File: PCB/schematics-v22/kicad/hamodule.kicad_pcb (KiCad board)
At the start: 2 copper layers, 78.4 x 84.3 mm, 91 parts, among them J1 GND|5V, J10 Conn_01x02_Male, J11 USB_C_Receptacle_USB2.0, J12 2604-1104, J13 EspSense, J2 2604-1102, J3 Conn_01x02_Male, J4 USB | PS, J5 Conn_01x02_Male, J6 GND|3.3V, J7 Current Jumper, J8 EspRelays, J9 2604-1104, K1 AQG12205, K2 AQG12205, K3 AQG12205, K4 AQG12205, SW1 Switch, SW2 Switch, U1 LD1117AV33, U2 ESP32-S3-WROOM-2, U3 ULN2003A, U4 USBLC6-2SC6, U5 LDA210-PDIP, U6 LDA210-PDIP, U7 SHT4x

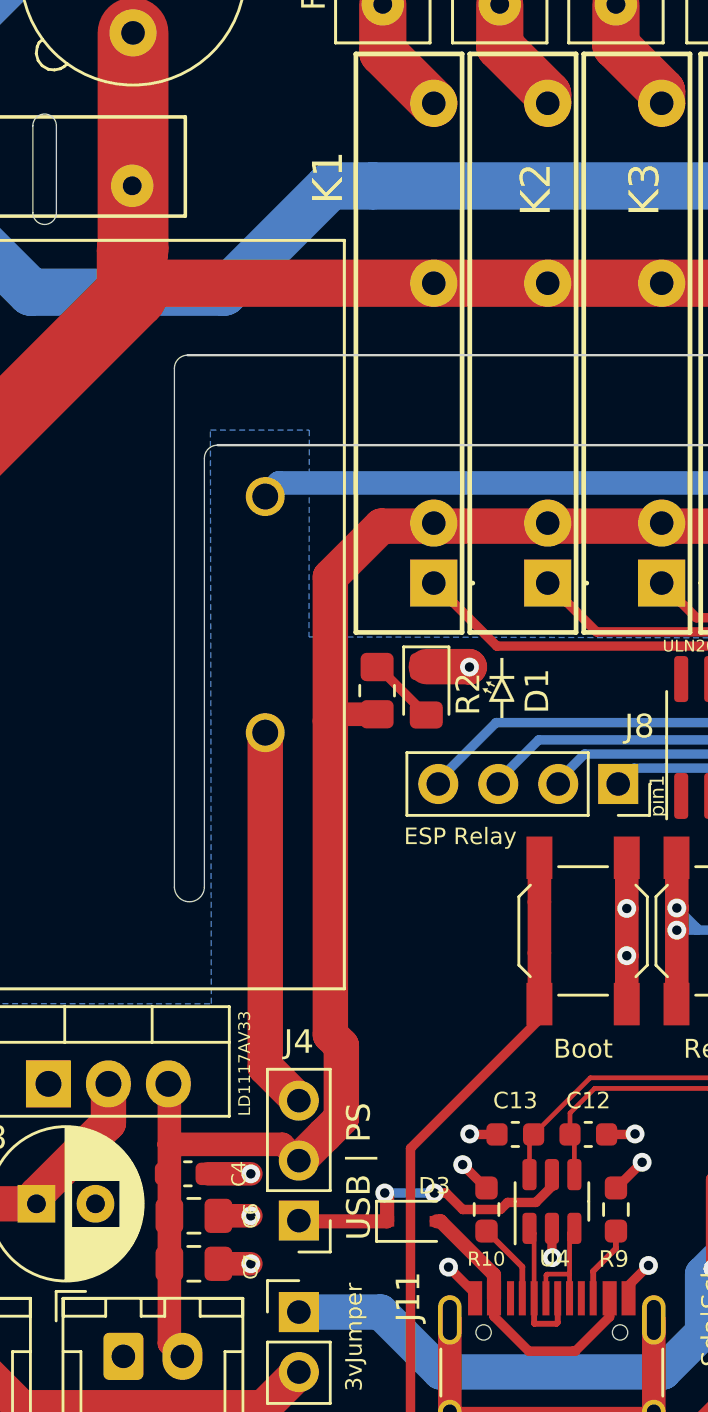
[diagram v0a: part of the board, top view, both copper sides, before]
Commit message: improving schematics, removing global variables and use wires instead to make it clear how the circuit is working; trying to move inputs to the left, output to the right
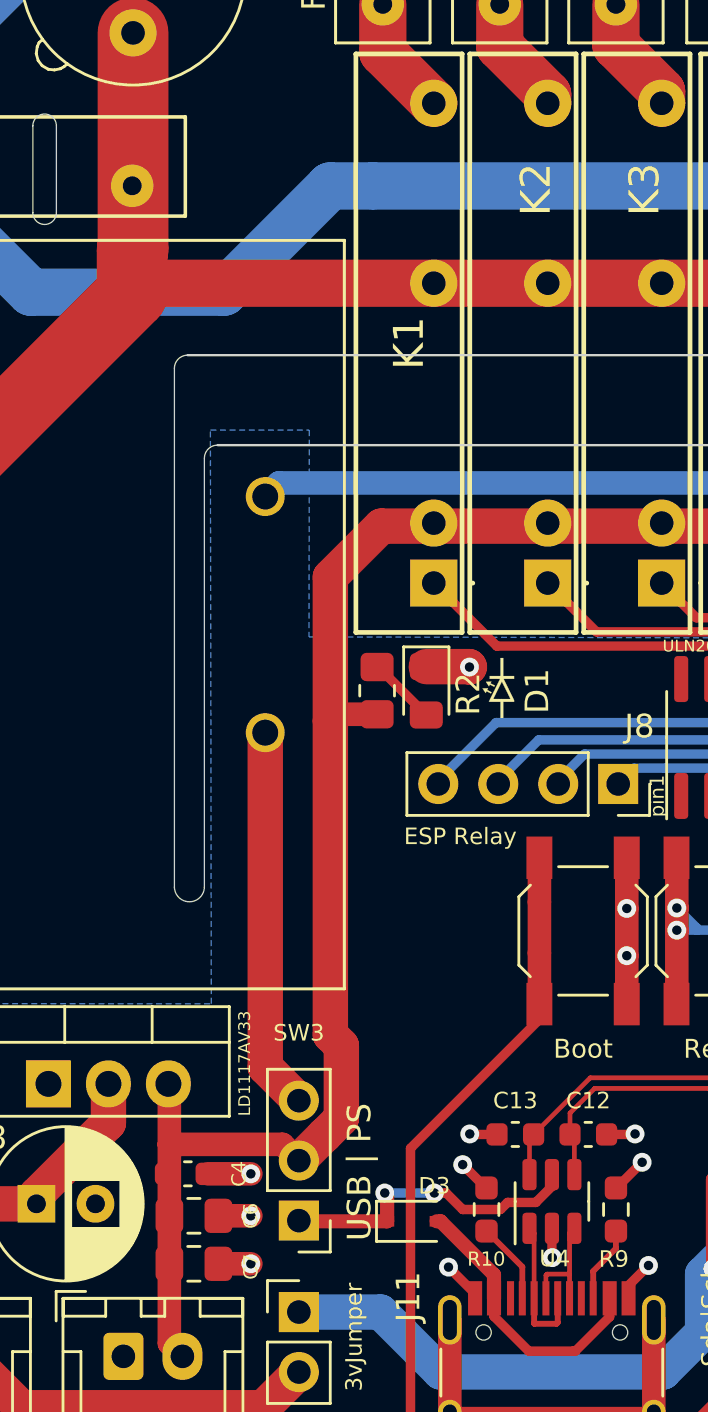
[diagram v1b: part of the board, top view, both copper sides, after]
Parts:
- removed J4: USB | PS, Connector_PinHeader_2.54mm:PinHeader_1x03_P2.54mm_Vertical
- added SW3: USB | PS, Connector_PinHeader_2.54mm:PinHeader_1x03_P2.54mm_Vertical, F.Cu at (56.3, 104.5)
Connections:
- net L_INPUT renamed Net-(F1-Pad1)
- net REI1 renamed Net-(U3-Pad13)
- net REI2 renamed Net-(K2-Pad1)
- net REI3 renamed Net-(K3-Pad1)
- net REI4 renamed Net-(K4-Pad1)
- net REO1 renamed Net-(F2-Pad1)
- net REO2 renamed Net-(F3-Pad1)
- net REO3 renamed Net-(F4-Pad1)
- net REO4 renamed Net-(F5-Pad1)
- net Sens1 renamed Net-(J12-Pad7)
- net Sens2 renamed Net-(J12-Pad5)
- net Sens3 renamed Net-(F8-Pad2)
- net Sens4 renamed Net-(J12-Pad1)
- net USB-D+ renamed Net-(J11-PadA6)
- net USB-D- renamed Net-(J11-PadA7)

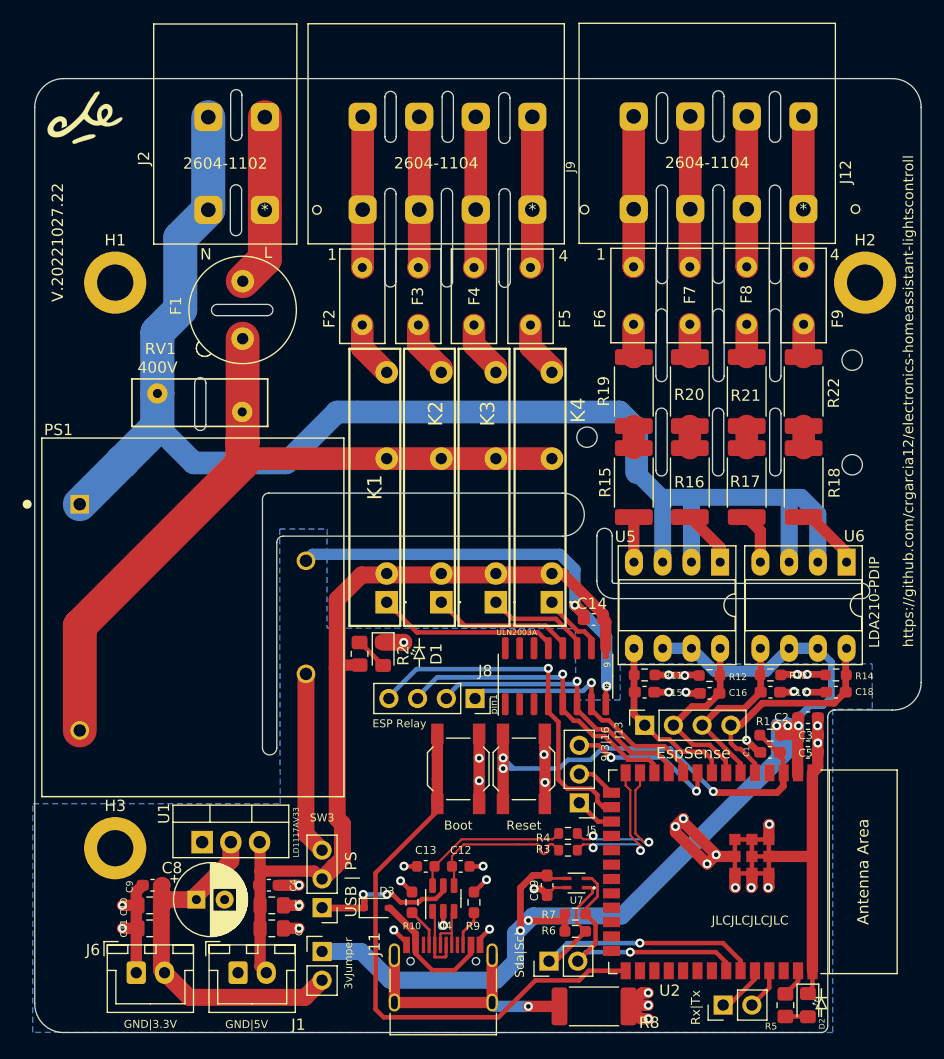
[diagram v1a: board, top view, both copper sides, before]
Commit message: [V22] Making schematics cleaner + Production files
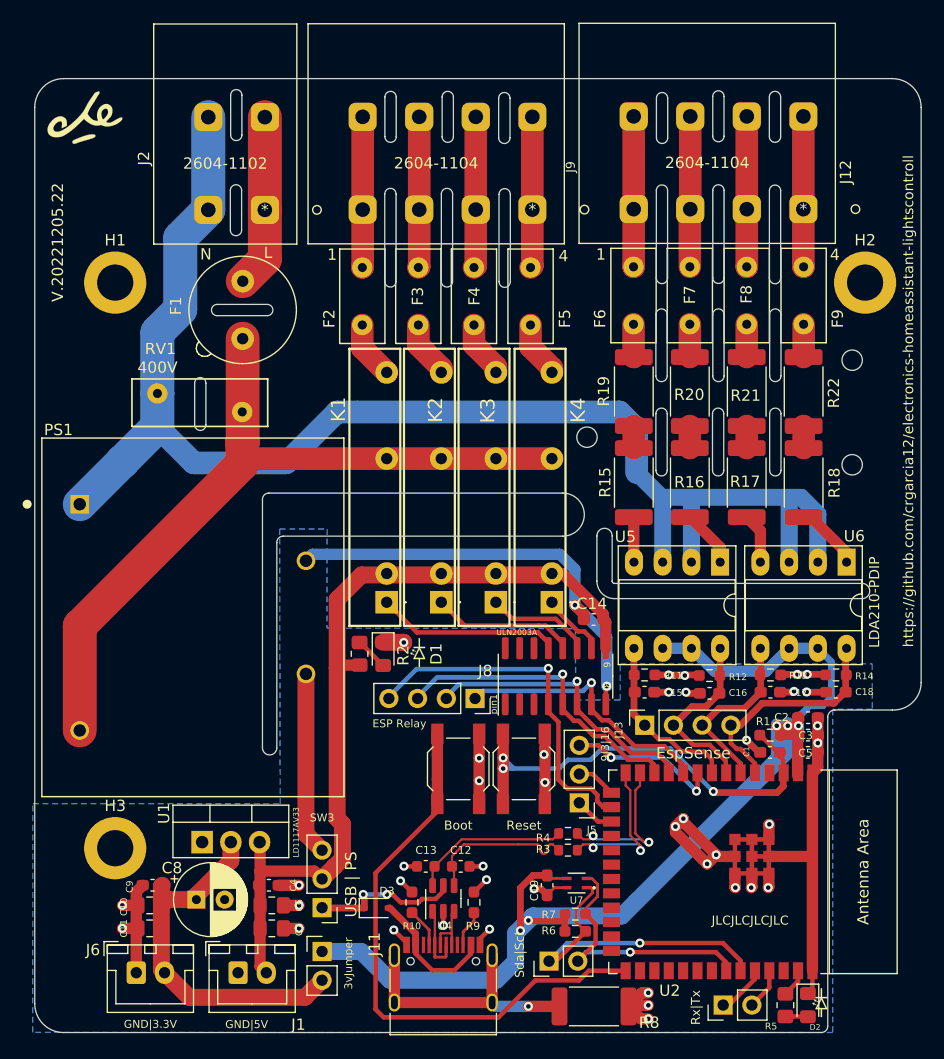
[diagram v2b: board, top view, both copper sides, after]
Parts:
- J10: value Conn_01x02_Male -> Serial
- J3: value Conn_01x02_Male -> Ì2C
- J5: value Conn_01x02_Male -> GPIOs
- turned C13 to 180 degrees
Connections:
- C13 pad 1: GND -> D-
- C13 pad 2: D- -> GND
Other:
- board text added: "V.20221205.22"
- board text removed: "V.20221027.22"

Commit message: adding leds to indicate relays operation
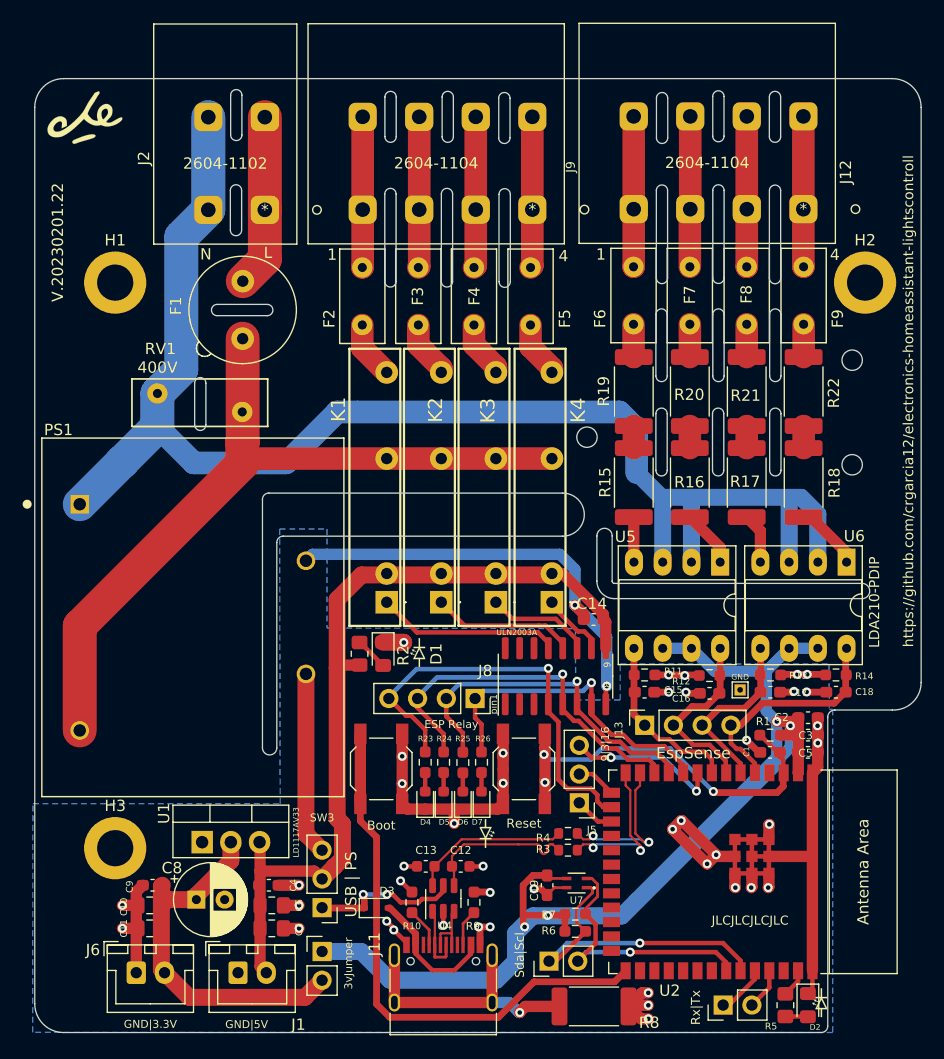
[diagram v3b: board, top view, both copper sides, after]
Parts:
- added D4: LED, LED_SMD:LED_0603_1608Metric, F.Cu at (65.4, 95.0)
- added D5: LED, LED_SMD:LED_0603_1608Metric, F.Cu at (67.0, 95.0)
- added D6: LED, LED_SMD:LED_0603_1608Metric, F.Cu at (68.7, 95.0)
- added D7: LED, LED_SMD:LED_0603_1608Metric, F.Cu at (70.4, 95.0)
- added G2: LOGO, icons:led_6000dpi, F.Cu at (70.9, 97.9)
- added R23: 100Ω, Resistor_SMD:R_0603_1608Metric_Pad0.98x0.95mm_HandSolder, F.Cu at (65.4, 91.6)
- added R24: 100Ω, Resistor_SMD:R_0603_1608Metric_Pad0.98x0.95mm_HandSolder, F.Cu at (67.0, 91.6)
- added R25: 100Ω, Resistor_SMD:R_0603_1608Metric_Pad0.98x0.95mm_HandSolder, F.Cu at (68.7, 91.6)
- added R26: 100Ω, Resistor_SMD:R_0603_1608Metric_Pad0.98x0.95mm_HandSolder, F.Cu at (70.4, 91.6)
- added TP1: GND, TestPoint:TestPoint_THTPad_1.0x1.0mm_Drill0.5mm, F.Cu at (93.2, 85.2)
- moved SW2 6.81 mm to (61.5, 92.2)
- turned SW1 to -90 degrees
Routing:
- net GND: track 166.5 -> 179.0 mm, vias 42 -> 45
- net 3.3V+: track 111.4 -> 100.6 mm, vias 5 -> 4
- net EspRel1: track 31.4 -> 37.7 mm
- net EspRel2: track 27.9 -> 33.5 mm
- net EspRel3: track 25.7 -> 31.0 mm
- net EspRel4: track 24.3 -> 29.5 mm
- net Net-(J11-PadS1): track 23.1 -> 27.4 mm
- net EN: track 40.3 -> 37.9 mm
- net IO0: track 50.7 -> 48.7 mm
- net Net-(D4-Pad2): track 0.00 -> 1.68 mm
- net Net-(D7-Pad2): track 0.00 -> 1.68 mm
- net Net-(D5-Pad2): track 0.00 -> 1.68 mm
- net Net-(D6-Pad2): track 0.00 -> 1.66 mm
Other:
- board text added: "V.20230201.22"
- board text removed: "V.20221205.22"

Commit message: Use VBus for ESD before BAT diode; Adding 2 more GPIO; Adding more caps
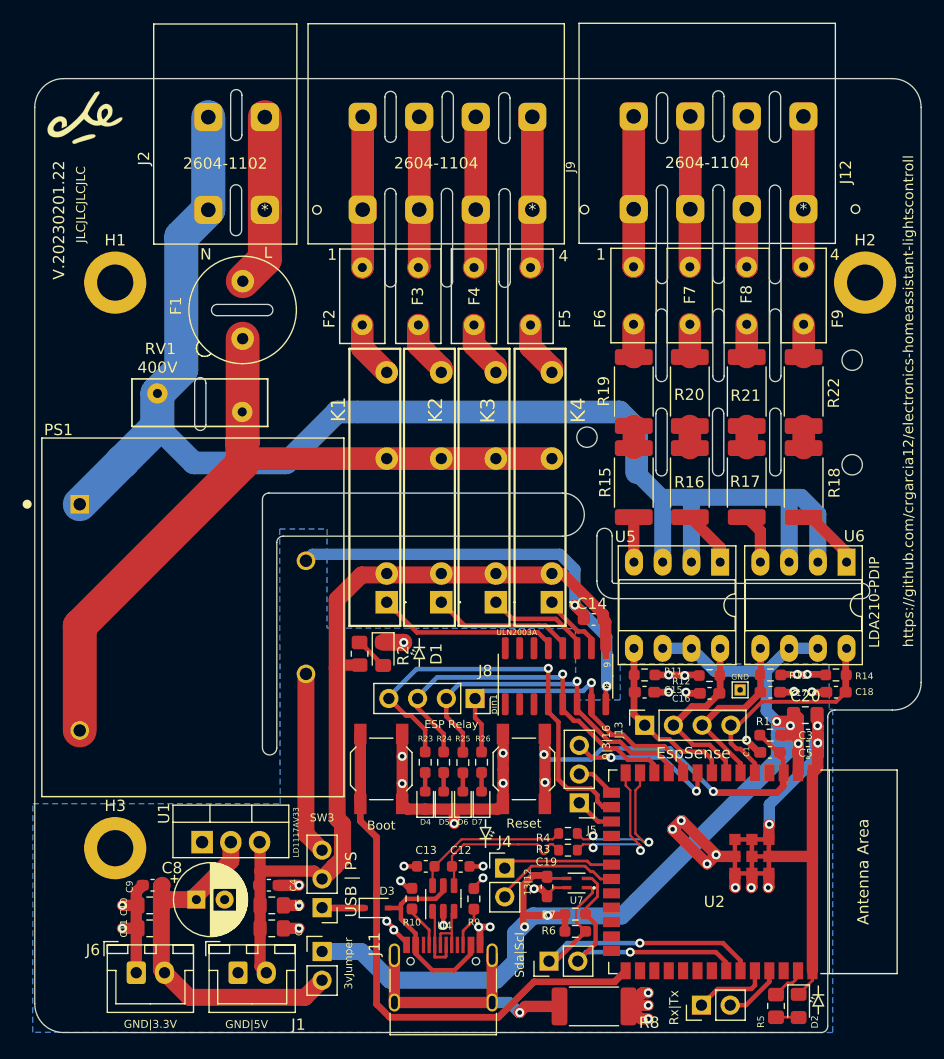
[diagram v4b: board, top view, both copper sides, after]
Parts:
- added C20: NC, Capacitor_SMD:C_0805_2012Metric_Pad1.18x1.45mm_HandSolder, F.Cu at (99.0, 87.5)
- added J4: 13|12, Connector_PinHeader_2.54mm:PinHeader_1x02_P2.54mm_Vertical, F.Cu at (72.4, 101.0)
- C2: footprint Capacitor_SMD:C_0603_1608Metric_Pad1.08x0.95mm_HandSolder -> Capacitor_SMD:C_1206_3216Metric_Pad1.33x1.80mm_HandSolder; moved to B.Cu
- J3: value Ì2C -> I2C
- J5: value GPIOs -> 9|3|16
- moved C2 2.74 mm to (98.4, 90.3)
- moved J10 1.92 mm to (89.8, 113.1)
- moved R5 0.83 mm to (96.4, 113.2)
- moved D2 0.82 mm to (98.4, 113.2)
- moved G2 0.36 mm to (100.0, 112.6)
- moved R10 0.33 mm to (64.2, 103.7)
- moved R9 0.31 mm to (69.7, 103.7)
- moved C19 0.11 mm to (76.2, 102.6)
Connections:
- D3 pad 2: Net-(D3-Pad2) -> Net-(U4-Pad5)
- J11 pad A4: Net-(D3-Pad2) -> Net-(U4-Pad5)
- J11 pad A9: Net-(D3-Pad2) -> Net-(U4-Pad5)
- J11 pad B4: Net-(D3-Pad2) -> Net-(U4-Pad5)
- J11 pad B9: Net-(D3-Pad2) -> Net-(U4-Pad5)
- U2 pad 20: unconnected-(U2-Pad20) -> GPIO12
- U2 pad 21: unconnected-(U2-Pad21) -> GPIO13
- U4 pad 5: VBUS -> Net-(U4-Pad5)
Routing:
- net Net-(U4-Pad5): track 0.00 -> 17.7 mm
- net Net-(D3-Pad2): track 12.0 -> 0.00 mm
- net GPIO13: track 0.00 -> 11.2 mm
- net GND: track 179.0 -> 189.1 mm
- net GPIO12: track 0.00 -> 9.67 mm
- net VBUS: track 13.3 -> 3.75 mm, vias 2 -> 0
- net 3.3V+: track 100.6 -> 109.6 mm, vias 4 -> 5
- net RXD0: track 4.49 -> 6.74 mm
- net TXD0: track 3.67 -> 5.29 mm
- net LED-GPIO: track 2.50 -> 3.16 mm
